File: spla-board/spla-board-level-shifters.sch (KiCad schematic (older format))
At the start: 19 parts

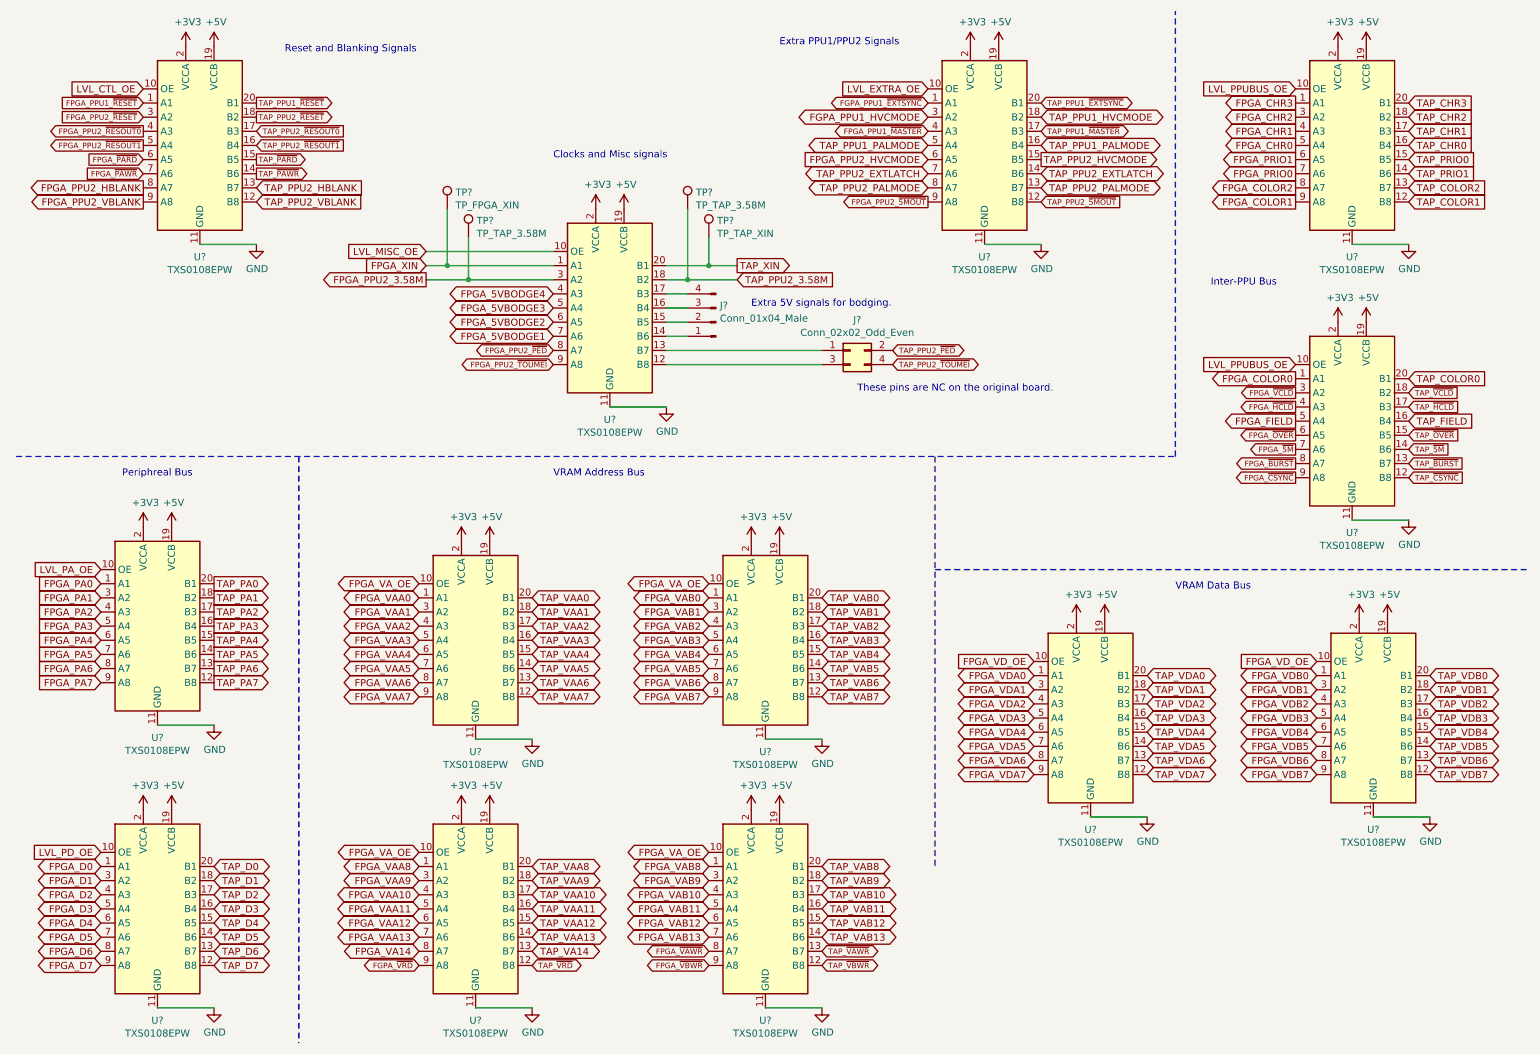
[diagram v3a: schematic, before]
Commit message: schematic: Move around a bunch of IC labels.
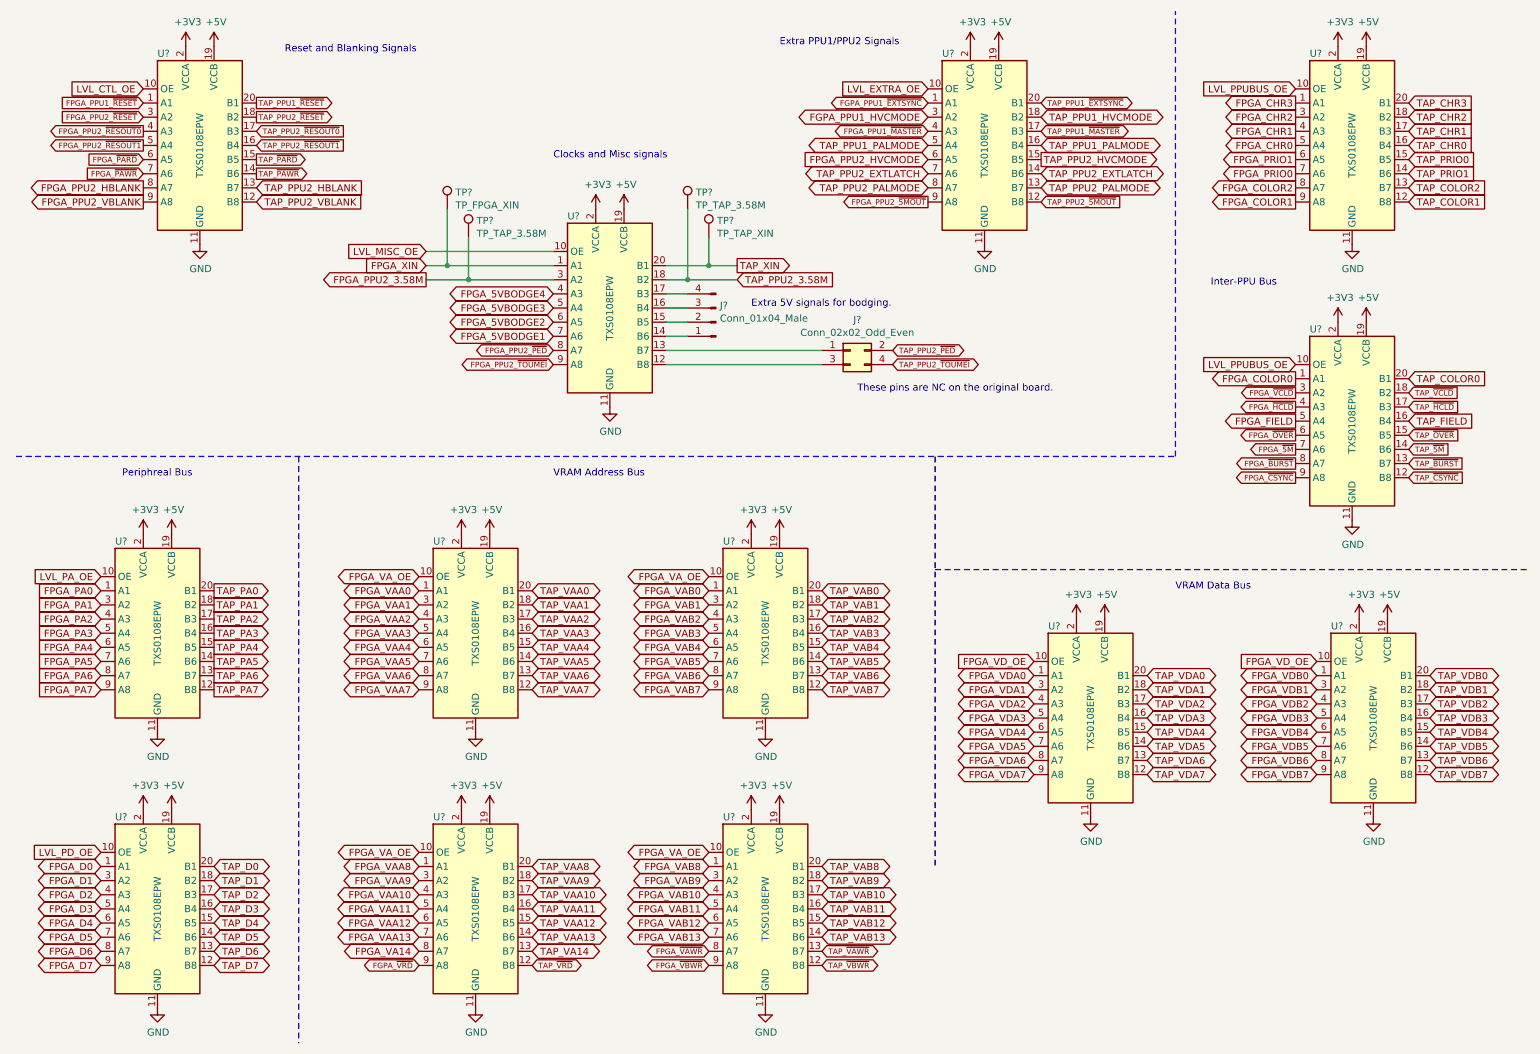
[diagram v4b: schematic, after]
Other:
- moved on the sheet: U?

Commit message: schematic: Change all pages to A3; open up layout for level shifters.
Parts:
- removed J?: Conn_01x04_Male, symbol Connector:Conn_01x04_Male
- added J?: Conn_01x04, symbol Connector_Generic:Conn_01x04
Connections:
- net FPGA_5VBODGE1: now also U?.4 (A3); no longer U?.7 (A6)
- net FPGA_5VBODGE2: now also U?.5 (A4); no longer U?.6 (A5)
- net FPGA_5VBODGE3: now also U?.6 (A5); no longer U?.5 (A4)
- net FPGA_5VBODGE4: now also U?.7 (A6); no longer U?.4 (A3)
- net at U?.14 (B6): now also J?.4 (Pin_4)
- net at U?.15 (B5): now also J?.3 (Pin_3)
- net at U?.16 (B4): now also J?.2 (Pin_2)
- net at U?.17 (B3): now also J?.1 (Pin_1)
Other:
- note added: "TODO: Consider adding decoupling capacitors to all these chips.\n"
- moved on the sheet: J?, TP?, U?
